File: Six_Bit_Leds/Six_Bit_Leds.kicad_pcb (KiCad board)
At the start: 2 copper layers, 15.2 x 29.2 mm, 11 parts, among them J1 Conn_01x06, J2 PwrGndL, J3 PwrGndR, U1 SN74AHC05N

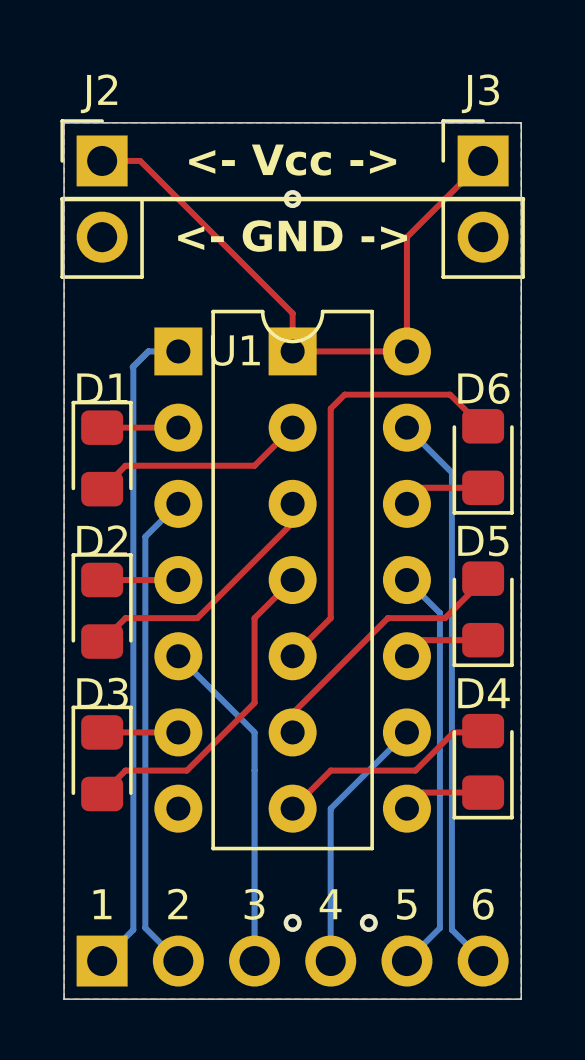
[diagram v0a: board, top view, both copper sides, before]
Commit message: v1.0 of STLink-MIPI-14-to-SWD-10
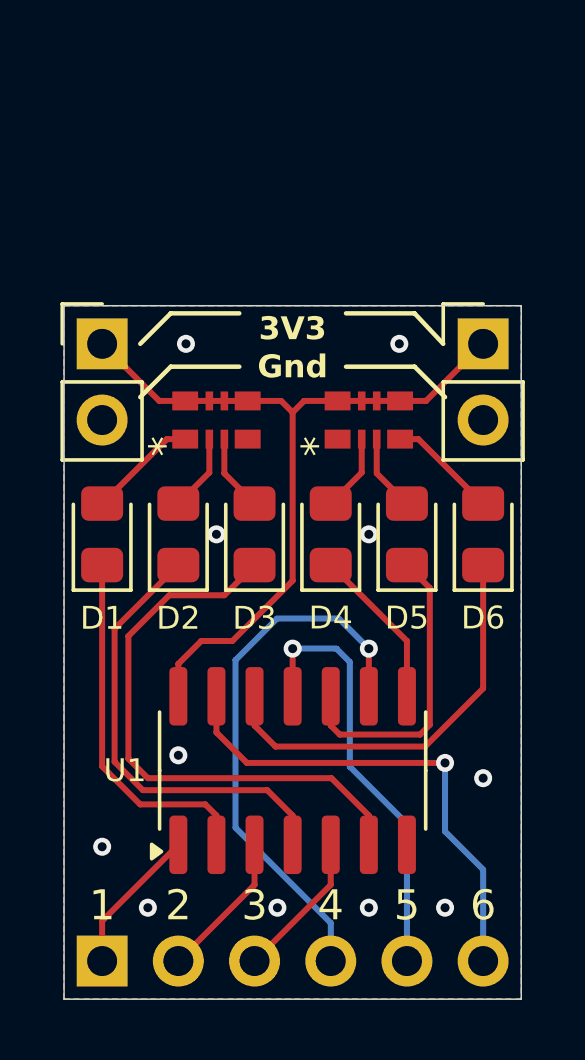
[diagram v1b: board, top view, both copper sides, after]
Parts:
- added RN2: R_Pack04, Project_Library:C_ARRAY_EXB28V_PAN, F.Cu at (135.9, 106.4)
- RN1: value 120R -> R_Pack04; footprint Resistor_THT:R_Array_SIP7 -> Project_Library:C_ARRAY_EXB28V_PAN; moved to F.Cu
- U1: footprint Package_DIP:DIP-14_W7.62mm -> Package_SO:SO-14_3.9x8.65mm_P1.27mm
- moved U1 14.5 mm to (133.3, 118.1), turned to 90 degrees
- moved D3 9.17 mm to (132.1, 110.2), turned to 90 degrees
- moved D4 9.13 mm to (134.6, 110.2)
- moved J2 6.10 mm to (127.0, 103.9)
- moved J3 6.10 mm to (139.7, 103.9)
- moved D2 3.60 mm to (129.5, 110.2), turned to 90 degrees
- moved D5 3.57 mm to (137.2, 110.2)
- moved RN1 3.42 mm to (130.8, 106.4), turned to 90 degrees
- moved D6 2.58 mm to (139.7, 110.2)
- moved D1 2.53 mm to (127.0, 110.2), turned to 90 degrees
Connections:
- RN1 pad 1: +3.3V -> Net-(D1-A)
- RN1 pad 2: Net-(D1-A) -> Net-(D2-A)
- RN1 pad 3: Net-(D2-A) -> Net-(D3-A)
- RN1 pad 4: Net-(D3-A) -> unconnected-(RN1-R4.1-Pad4)
- RN1 pad 5: Net-(D6-A) -> +3.3V
- RN1 pad 6: Net-(D5-A) -> +3.3V
- RN1 pad 7: Net-(D4-A) -> +3.3V
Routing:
- net /IN1: track 22.7 -> 4.93 mm
- net /LED3: track 2.54 -> 19.0 mm
- net /LED2: track 2.54 -> 15.1 mm
- net /IN2: track 16.2 -> 4.93 mm
- net /LED6: track 2.76 -> 13.8 mm
- net Net-(D6-A): track 14.5 -> 3.66 mm
- net /IN4: track 8.67 -> 18.4 mm, vias 0 -> 1
- net /LED1: track 2.54 -> 12.2 mm
- net Net-(D3-A): track 11.0 -> 2.56 mm
- net /LED5: track 2.76 -> 10.2 mm
- net /IN3: track 11.2 -> 4.93 mm
- net Net-(D5-A): track 8.83 -> 2.56 mm
- net Net-(D2-A): track 8.62 -> 2.58 mm
- net +3.3V: track 20.9 -> 26.2 mm
- net Net-(D4-A): track 7.45 -> 2.58 mm
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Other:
- board size 15.2 x 29.2 mm -> 15.2 x 23.1 mm
- board text added: "${FILENAME} ${REVISION} ${ISSUE_DATE} ${COMPANY}"
- board text added: "3V3"
- board text added: "Gnd"
- board text removed: "${FILENAME}, ${REVISION}"
- board text removed: "<- GND ->"
- board text removed: "<- Vcc ->"
